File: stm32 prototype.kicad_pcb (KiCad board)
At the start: 4 copper layers, 137 x 54.5 mm, 114 parts, among them J1 USB_B_Mini, J2 Conn_01x06, J3 Conn_02x08_Odd_Even, J4 Conn_01x10, J5 Conn_02x04_Odd_Even, J6 Conn_01x15, J7 Conn_01x15, Q1 Q_NMOS_GSD, Q10 2N2219, Q11 Q_NMOS_GSD, Q2 Q_NMOS_GSD, Q3 Q_NMOS_GSD, Q4 Q_NMOS_GSD, Q5 Q_NMOS_GSD, Q6 Q_NMOS_GSD, Q7 Q_NMOS_GSD, Q8 Q_NMOS_GSD, Q9 2N2219, SW1 SW_Push, SW2 SW_Push, U1 FT232RL, U2 W25Q128JV-DTR, U3 STM32F407VGTx, U4 LD1117S33TR, U5 ESP32-WROOM, U7 TPS62203DBVR, Y1 Crystal_GND24

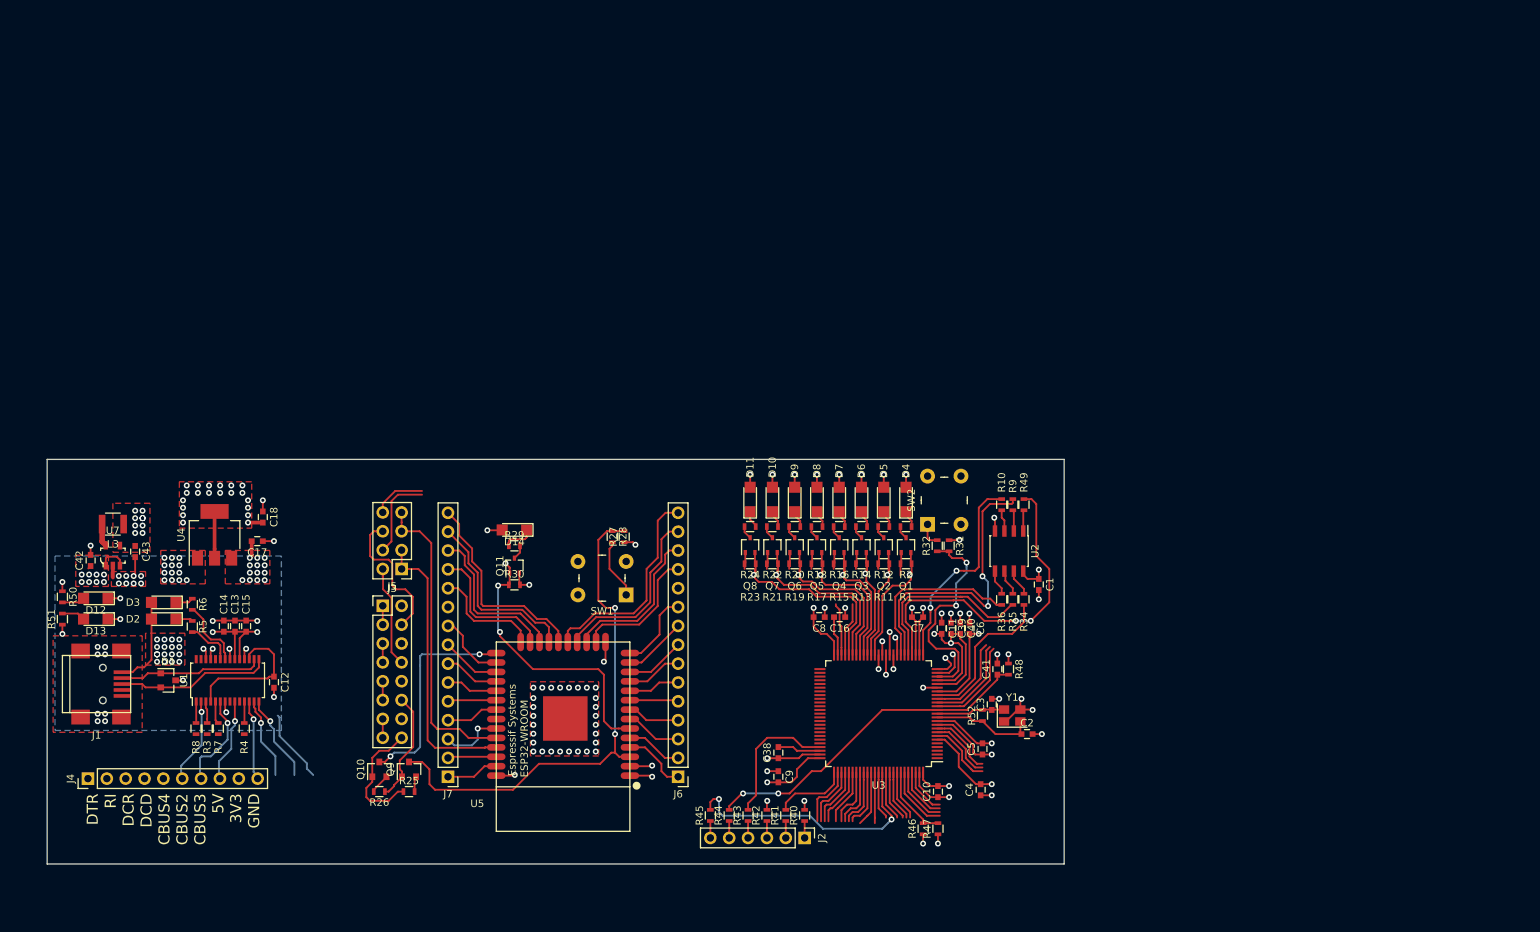
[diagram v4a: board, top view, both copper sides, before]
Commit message: layout almost done, changing my mind, getting rid of esp32, usb section
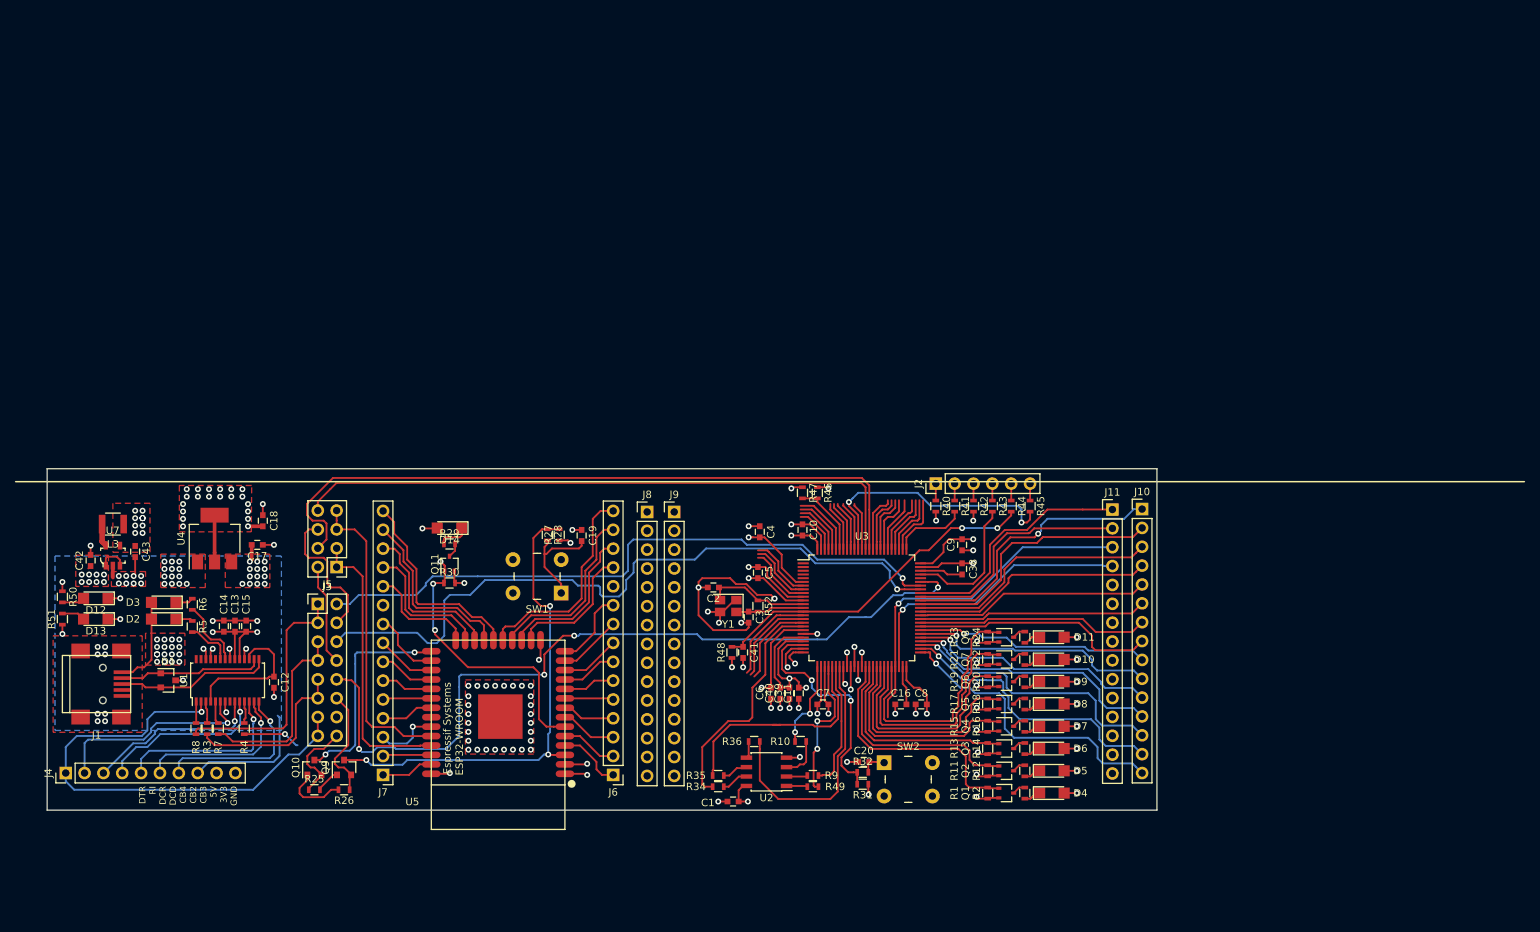
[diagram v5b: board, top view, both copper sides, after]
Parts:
- added C19: 0.1uF, Capacitors_SMD:C_0603, F.Cu at (134.5, 98.2)
- added C20: 0.1uF, Capacitors_SMD:C_0603, F.Cu at (172.5, 128.8)
- added J10: Conn_01x15, Pin_Headers:Pin_Header_Straight_1x15_Pitch2.54mm, F.Cu at (210.0, 94.7)
- added J11: Conn_01x15, Pin_Headers:Pin_Header_Straight_1x15_Pitch2.54mm, F.Cu at (206.0, 94.8)
- added J8: Conn_01x15, Pin_Headers:Pin_Header_Straight_1x15_Pitch2.54mm, F.Cu at (143.3, 95.1)
- added J9: Conn_01x15, Pin_Headers:Pin_Header_Straight_1x15_Pitch2.54mm, F.Cu at (147.0, 95.1)
- Q10, Q9: value 2N2219 -> Q_NPN_BEC
- R25, R26: value 12k -> 10k
- moved R45 59.9 mm to (194.9, 94.3), turned to 270 degrees
- moved R44 56.4 mm to (192.4, 94.3), turned to 270 degrees
- moved R43 53.1 mm to (189.8, 94.3), turned to 270 degrees
- moved J2 50.9 mm to (182.2, 91.3), turned to 90 degrees
- moved C1 50.5 mm to (154.9, 134.1), turned to 180 degrees
- moved R42 50.1 mm to (187.3, 94.3), turned to 270 degrees
- moved R47 48.8 mm to (164.2, 92.5), turned to 270 degrees
- moved R34 48.3 mm to (152.9, 132.1), turned to 0 degrees
- moved R41 47.5 mm to (184.8, 94.3), turned to 270 degrees
- moved R49 47.5 mm to (165.7, 132.1), turned to 180 degrees
- moved R46 47.4 mm to (166.2, 92.5), turned to 270 degrees
- moved C2 46.6 mm to (152.2, 105.2), turned to 180 degrees
- moved R35 46.2 mm to (152.9, 130.6), turned to 0 degrees
- moved C4 45.7 mm to (158.5, 97.8), turned to 270 degrees
- moved R9 45.4 mm to (165.7, 130.6), turned to 180 degrees
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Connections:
- Q10 pad 1: FTDI_ES_DTR -> Net-(Q10-Pad1)
- Q10 pad 2: Net-(Q10-Pad2) -> FTDI_ES_DTR
- Q9 pad 1: FTDI_ES_RTS -> Net-(Q9-Pad1)
- Q9 pad 2: Net-(Q9-Pad2) -> FTDI_ES_RTS
- R25 pad 2: Net-(Q9-Pad2) -> Net-(Q9-Pad1)
- R26 pad 2: Net-(Q10-Pad2) -> Net-(Q10-Pad1)
- R7 pad 1: FTDI_ST_RXD -> Net-(R7-Pad1)
- R7 pad 2: Net-(R7-Pad2) -> Net-(J3-Pad5)
- R8 pad 1: FTDI_ST_TXD -> Net-(R8-Pad1)
- R8 pad 2: Net-(R8-Pad2) -> Net-(J3-Pad1)
- U1 pad 1: Net-(J3-Pad1) -> Net-(R8-Pad1)
- U1 pad 5: Net-(J3-Pad5) -> Net-(R7-Pad1)
- U3 pad 47: (no net) -> PB10
- U3 pad 48: (no net) -> PB11
- U3 pad 51: (no net) -> PB12
- U3 pad 52: (no net) -> PB13
- U3 pad 53: (no net) -> PB14
- U3 pad 54: (no net) -> PB15
- U3 pad 55: (no net) -> PD8
- U3 pad 56: (no net) -> PD9
- U3 pad 57: (no net) -> PD10
- U3 pad 58: (no net) -> PD11
- U3 pad 59: (no net) -> PD12
- U3 pad 60: (no net) -> PD13
- U3 pad 61: (no net) -> PD14
- U3 pad 62: (no net) -> PD15
- U3 pad 63: (no net) -> PC6
- U3 pad 64: (no net) -> PC7
- U3 pad 65: (no net) -> PC8
- U3 pad 66: (no net) -> PC9
- U3 pad 67: (no net) -> PA8
- U3 pad 68: Net-(R7-Pad2) -> FTDI_ST_RXD
- U3 pad 69: Net-(R8-Pad2) -> FTDI_ST_TXD
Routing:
- net FTDI_ST_RTS: track 0.00 -> 109.1 mm, vias 0 -> 4
- net FTDI_ST_RXD: track 0.00 -> 94.7 mm, vias 0 -> 1
- net FTDI_ST_TXD: track 0.00 -> 87.5 mm, vias 0 -> 1
- net ST_ESP_RXD: track 19.0 -> 94.6 mm
- net ST_ESP_TXD: track 14.0 -> 84.6 mm
- net Net-(J3-Pad13): track 2.54 -> 67.2 mm, vias 0 -> 1
- net PB10: track 0.00 -> 47.9 mm, vias 0 -> 1
- net PB12: track 0.00 -> 40.2 mm, vias 0 -> 1
- net PB11: track 0.00 -> 38.6 mm, vias 0 -> 1
- net PB13: track 0.00 -> 38.3 mm, vias 0 -> 1
- net PC8: track 0.00 -> 37.6 mm, vias 0 -> 1
- net PB14: track 0.00 -> 37.2 mm, vias 0 -> 1
- net PC7: track 0.00 -> 36.2 mm
- net PB15: track 0.00 -> 35.4 mm, vias 0 -> 1
- net PC6: track 0.00 -> 34.3 mm
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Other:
- board size 137 x 54.5 mm -> 149.5 x 46 mm
- board text added: "DTR RI DCR DCD CB4 CB2 CB3 5V 3V3 GND"
- board text removed: "DTR RI DCR DCD CBUS4 CBUS2 CBUS3 5V 3V3 GND"

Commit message: Ordered PCB 12/18
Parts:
- removed C12, C13, C14, C15: C, Capacitors_SMD:C_0603
- removed C19: 0.1uF, Capacitors_SMD:C_0603
- removed D1: SP0502BAHT, TO_SOT_Packages_SMD:SOT-23
- removed D14, D2, D3: LED, LEDs:LED_1206
- removed J8: Conn_01x15, Pin_Headers:Pin_Header_Straight_1x15_Pitch2.54mm
- removed Q10, Q9: Q_NPN_BEC, TO_SOT_Packages_SMD:SOT-23
- removed Q11: Q_NMOS_GSD, TO_SOT_Packages_SMD:SOT-323_SC-70
- removed R25, R26: 10k, Resistors_SMD:R_0603
- removed R27: 12k, Resistors_SMD:R_0603
- removed R28: 470R, Resistors_SMD:R_0603
- removed R29, R5, R6: 330R, Resistors_SMD:R_0603
- removed R30: 10K, Resistors_SMD:R_0603
- removed R7, R8: 0R, Resistors_SMD:R_0603
- removed SW1: SW_Push, switches_mdg:Switch_Tactile_6x6mm_Vertical_SMD_MJTP1230
- removed U1: FT232RL, Housings_SSOP:TSSOP-28_4.4x9.7mm_Pitch0.65mm
- removed U5: ESP32-WROOM, ESP32-footprints-Lib:ESP32-WROOM
- added J12: Conn_01x07, Pin_Headers:Pin_Header_Straight_1x07_Pitch2.54mm, F.Cu at (203.2, 127.0)
- added J13: Conn_01x06, Pin_Headers:Pin_Header_Straight_1x06_Pitch2.54mm, F.Cu at (170.2, 127.0)
- added J14: Conn_01x30, Pin_Headers:Pin_Header_Straight_1x30_Pitch2.54mm, F.Cu at (139.7, 68.6)
- J1: value USB_B_Mini -> Conn_01x04; footprint Connectors:USB_Mini-B -> Pin_Headers:Pin_Header_Straight_1x04_Pitch2.54mm
- J10: value Conn_01x15 -> Conn_01x03; footprint Pin_Headers:Pin_Header_Straight_1x15_Pitch2.54mm -> Pin_Headers:Pin_Header_Straight_1x03_Pitch2.54mm
- J11: value Conn_01x15 -> Conn_01x05; footprint Pin_Headers:Pin_Header_Straight_1x15_Pitch2.54mm -> Pin_Headers:Pin_Header_Straight_1x05_Pitch2.54mm
- J3: value Conn_02x08_Odd_Even -> Conn_01x08; footprint Pin_Headers:Pin_Header_Straight_2x08_Pitch2.54mm -> Pin_Headers:Pin_Header_Straight_1x08_Pitch2.54mm
- J4: value Conn_01x10 -> Conn_01x06; footprint Pin_Headers:Pin_Header_Straight_1x10_Pitch2.54mm -> Pin_Headers:Pin_Header_Straight_1x06_Pitch2.54mm
- J5: value Conn_02x04_Odd_Even -> Conn_01x06; footprint Pin_Headers:Pin_Header_Straight_2x04_Pitch2.54mm -> Pin_Headers:Pin_Header_Straight_1x06_Pitch2.54mm
- J6, J7: value Conn_01x15 -> Conn_01x06; footprint Pin_Headers:Pin_Header_Straight_1x15_Pitch2.54mm -> Pin_Headers:Pin_Header_Straight_1x06_Pitch2.54mm
- J9: value Conn_01x15 -> Conn_01x08; footprint Pin_Headers:Pin_Header_Straight_1x15_Pitch2.54mm -> Pin_Headers:Pin_Header_Straight_1x08_Pitch2.54mm
- R3, R4: value 0R -> 10K
- moved J4 144.0 mm to (207.6, 110.3), turned to 0 degrees
- moved R3 137.8 mm to (220.5, 105.0), turned to 270 degrees
- moved R4 130.8 mm to (218.8, 107.5), turned to 0 degrees
- moved J7 112.6 mm to (218.5, 110.3), turned to 0 degrees
- moved J5 110.0 mm to (211.2, 110.3), turned to 0 degrees
- moved D12 85.2 mm to (154.3, 105.9)
- moved D13 85.2 mm to (154.3, 108.7)
- moved R50 85.2 mm to (149.8, 105.7)
- moved R51 85.2 mm to (149.8, 108.7)
- moved J6 78.8 mm to (214.9, 110.3), turned to 0 degrees
- moved C1 75.8 mm to (202.1, 74.7), turned to 0 degrees
- moved R34 75.4 mm to (204.1, 76.7), turned to 180 degrees
- moved C42 74.7 mm to (143.0, 98.4), turned to 180 degrees
- moved U7 73.8 mm to (144.9, 95.2), turned to 90 degrees
- moved J9 73.3 mm to (219.0, 81.7)
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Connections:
- net ST_MISO renamed SPI1_MISO
- net ST_MOSI renamed SPI1_MOSI
- net ST_SCK renamed SPI1_SCK
- J1 pad 1: +5V -> GND
- J1 pad 2: Net-(D1-Pad1) -> (no net)
- J1 pad 3: Net-(D1-Pad2) -> FTDI_ST_TXD
- J1 pad 4: (no net) -> FTDI_ST_RXD
- J10 pad 1: PC8 -> PD0
- J10 pad 2: PC7 -> PD1
- J10 pad 3: PC6 -> PD2
- J11 pad 1: PA8 -> PB4
- J11 pad 2: PC9 -> PB8
- J11 pad 3: PB10 -> PB9
- J11 pad 4: PB11 -> PE0
- J11 pad 5: (no net) -> PE1
- J3 pad 1: Net-(J3-Pad1) -> +5V
- J3 pad 2: FTDI_ST_TXD -> (no net)
- J3 pad 3: Net-(J3-Pad1) -> (no net)
- J3 pad 4: FTDI_ES_TXD -> (no net)
- J3 pad 5: Net-(J3-Pad5) -> (no net)
- J3 pad 6: FTDI_ST_RXD -> FTDI_ST_RTS
- J3 pad 7: Net-(J3-Pad5) -> FTDI_CTS
- J3 pad 8: FTDI_ES_RXD -> GND
- J4 pad 1: Net-(J3-Pad13) -> I2C1_SDA
- J4 pad 2: FTDI_RI -> I2C1_SCL
- J4 pad 3: FTDI_DCR -> I2C1_SMBA
- J4 pad 4: FTDI_DCD -> +5V
- J4 pad 5: FTDI_CBUS4 -> +3V3
- J4 pad 6: FTDI_CBUS2 -> GND
- J5 pad 1: Net-(J5-Pad1) -> I2C1_SDA
- J5 pad 2: FTDI_ES_RXD -> I2C1_SCL
- J5 pad 3: Net-(J5-Pad1) -> I2C1_SMBA
- J5 pad 4: ST_ESP_RXD -> +5V
- J5 pad 5: Net-(J5-Pad5) -> +3V3
- J5 pad 6: FTDI_ES_TXD -> GND
- J6 pad 1: SENSOR_VP -> I2C1_SDA
- J6 pad 2: SENSOR_VN -> I2C1_SCL
- J6 pad 3: IO35 -> I2C1_SMBA
- J6 pad 4: IO32 -> +5V
- J6 pad 5: IO33 -> +3V3
- J6 pad 6: IO25 -> GND
- J7 pad 1: IO23 -> I2C1_SDA
- J7 pad 2: IO22 -> I2C1_SCL
- J7 pad 3: IO21 -> I2C1_SMBA
- J7 pad 4: IO19 -> +5V
- J7 pad 5: IO18 -> +3V3
- J7 pad 6: IO5 -> GND
- J9 pad 1: (no net) -> PC15
- J9 pad 2: (no net) -> PC14
- J9 pad 3: (no net) -> PC13
- J9 pad 4: (no net) -> PE6
- J9 pad 5: (no net) -> PE5
- J9 pad 6: (no net) -> PE4
- J9 pad 7: (no net) -> PE3
- J9 pad 8: (no net) -> PE2
- R3 pad 1: Net-(J3-Pad11) -> +3V3
- R3 pad 2: Net-(R3-Pad2) -> I2C1_SCL
- R4 pad 1: FTDI_CTS -> +3V3
- R4 pad 2: Net-(R4-Pad2) -> I2C1_SDA
- U3 pad 1: (no net) -> PE2
- U3 pad 15: (no net) -> PC0
- U3 pad 16: (no net) -> PC1
- U3 pad 17: (no net) -> PC2
- U3 pad 2: (no net) -> PE3
- U3 pad 24: (no net) -> PA1
- U3 pad 25: (no net) -> PA2
- U3 pad 3: (no net) -> PE4
- U3 pad 33: (no net) -> PC4
- U3 pad 34: (no net) -> PC5
- U3 pad 35: (no net) -> PB0
- U3 pad 36: (no net) -> PB1
- U3 pad 37: (no net) -> PB2
- U3 pad 38: (no net) -> PE7
- U3 pad 39: STATUS_BIT0 -> PE8
- U3 pad 4: (no net) -> PE5
- U3 pad 40: STATUS_BIT1 -> PE9
- U3 pad 41: STATUS_BIT2 -> PE10
- U3 pad 42: STATUS_BIT3 -> PE11
- U3 pad 43: STATUS_BIT4 -> PE12
- U3 pad 44: STATUS_BIT5 -> PE13
- U3 pad 45: STATUS_BIT6 -> PE14
- U3 pad 46: STATUS_BIT7 -> PE15
- U3 pad 5: (no net) -> PE6
- U3 pad 60: PD13 -> STATUS_BIT0
- U3 pad 61: PD14 -> STATUS_BIT1
- U3 pad 62: PD15 -> STATUS_BIT2
- U3 pad 63: PC6 -> STATUS_BIT3
- U3 pad 64: PC7 -> STATUS_BIT4
- U3 pad 65: PC8 -> STATUS_BIT5
- U3 pad 66: PC9 -> STATUS_BIT6
- U3 pad 67: PA8 -> STATUS_BIT7
- U3 pad 7: (no net) -> PC13
- U3 pad 77: (no net) -> SPI3_NSS
- U3 pad 78: (no net) -> SPI3_SCK
- U3 pad 79: (no net) -> SPI3_MISO
- U3 pad 8: (no net) -> PC14
- U3 pad 80: (no net) -> SPI3_MOSI
- U3 pad 81: (no net) -> PD0
- U3 pad 82: (no net) -> PD1
- U3 pad 83: (no net) -> PD2
- U3 pad 84: (no net) -> USART2_CTS
- U3 pad 85: (no net) -> USART2_RTS
- U3 pad 86: ST_ESP_RXD -> USART2_TX
- U3 pad 87: ST_ESP_TXD -> USART2_RX
- U3 pad 88: (no net) -> USART2_CK
- U3 pad 9: (no net) -> PC15
- U3 pad 90: (no net) -> PB4
- U3 pad 91: (no net) -> I2C1_SMBA
- U3 pad 92: (no net) -> I2C1_SCL
- U3 pad 93: (no net) -> I2C1_SDA
- U3 pad 95: (no net) -> PB8
- U3 pad 96: (no net) -> PB9
- U3 pad 97: (no net) -> PE0
- U3 pad 98: (no net) -> PE1
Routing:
- net (no net): track 220.7 -> 0.00 mm, vias 8 -> 0
- net ST_ESP_RXD: track 94.6 -> 0.00 mm
- net FTDI_ST_RTS: track 109.1 -> 24.2 mm, vias 4 -> 0
- net ST_ESP_TXD: track 84.6 -> 0.00 mm
- net Net-(J3-Pad13): track 67.2 -> 0.00 mm, vias 1 -> 0
- net ESP_EN: track 66.9 -> 0.00 mm, vias 3 -> 0
- net +5V: track 51.7 -> 116.1 mm, vias 42 -> 22
- net I2C1_SCL: track 0.00 -> 52.5 mm
- net PC15: track 0.00 -> 50.6 mm
- net PC14: track 0.00 -> 49.4 mm
- net FTDI_ST_RXD: track 94.7 -> 45.5 mm, vias 1 -> 0
- net I2C1_SDA: track 0.00 -> 48.7 mm
- net FTDI_ST_TXD: track 87.5 -> 39.9 mm, vias 1 -> 0
- net PE4: track 0.00 -> 47.3 mm, vias 0 -> 2
- net PC13: track 0.00 -> 46.8 mm
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- added copper zone on B.Cu, net GND
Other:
- board size 149.5 x 46 mm -> 86 x 64 mm
- rule pad_to_mask_clearance: 0.051 -> 0
- board text added: "5V"
- board text added: "GND X RXD TXD"
- board text added: "I2C1 SDA SCL SMBA 5V 3V3 GND"
- board text added: "PA1"
- board text added: "PA2"
- board text added: "PB0"
- board text added: "PB1"
- board text added: "PB10"
- board text added: "PB11"
- board text added: "PB12"
- board text added: "PB13"
- board text added: "PB14"
- board text added: "PB15"
- board text added: "PB2"
- board text added: "PB4 PB8 PB9 PE0 PE1"
- board text added: "PC0"
- board text added: "PC1"
- board text added: "PC2"
- board text added: "PC4"
- board text added: "PC5"
- board text added: "PD10"
- board text added: "PD11"
- board text added: "PD12"
- board text added: "PD2 PD1 PD0"
- board text added: "PD8"
- board text added: "PD9"
- board text added: "PE10"
- board text added: "PE11"
- board text added: "PE12"
- board text added: "PE13"
- board text added: "PE14"
- board text added: "PE15"
- board text added: "PE7"
- board text added: "PE8"
- board text added: "PE9"
- board text added: "RTS CTS GND"
- board text added: "SPI3 NSS SCK MISO MOSI 3V3 GND"
- board text added: "SWO NRST TMS_SDIO GND TCK_SWCK GND"
- board text added: "USART2 GND 3V3 CTS RTS TX RX CK"
- board text removed: "DTR RI DCR DCD CB4 CB2 CB3 5V 3V3 GND"

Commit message: pushed change to stm32f405 to pcb
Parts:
- removed J11: Conn_01x05, Pin_Headers:Pin_Header_Straight_1x05_Pitch2.54mm
- removed R10, R34, R35, R36, R40, R41, R42, R43, R44, R45, R49, R9: 0R, Resistors_SMD:R_0603
- removed U2: W25Q128JV-DTR, Housings_SOIC:SOIC-8_3.9x4.9mm_Pitch1.27mm
- removed U4: LD1117S33TR, TO_SOT_Packages_SMD:SOT-223
- added C12: 0.1uF, Capacitors_SMD:C_0603, F.Cu at (91.0, 84.8)
- added C13: 2.2uF, Capacitors_SMD:C_0603, F.Cu at (93.9, 84.8)
- added C14: 2.2uF, Capacitors_SMD:C_0603, F.Cu at (96.7, 84.8)
- added C15: 9pF, Capacitors_SMD:C_0603, F.Cu at (91.0, 86.2)
- added C19: .1uF, Capacitors_SMD:C_0603, F.Cu at (93.9, 86.2)
- added C21: .1uF, Capacitors_SMD:C_0603, F.Cu at (96.7, 86.2)
- added C22: .1uF, Capacitors_SMD:C_0603, F.Cu at (99.6, 84.8)
- added C23: .1uF, Capacitors_SMD:C_0603, F.Cu at (99.6, 86.2)
- added C24: .1uF, Capacitors_SMD:C_0603, F.Cu at (102.4, 84.8)
- added J8: Conn_ARM_JTAG_SWD_10, Pin_Headers:Pin_Header_Straight_2x05_Pitch1.27mm_SMD, F.Cu at (121.4, 65.8)
- added R5: 10k, Resistors_SMD:R_0603, F.Cu at (104.3, 77.4)
- added R6: 10k, Resistors_SMD:R_0603, F.Cu at (104.3, 78.9)
- added R7: 1MR, Resistors_SMD:R_0603, F.Cu at (104.3, 80.4)
- added R8: 10k, Resistors_SMD:R_0603, F.Cu at (104.3, 81.9)
- added SW1: SW_Push, switches_mdg:Switch_Tactile_6x6mm_Vertical_SMD_MJTP1230, F.Cu at (89.9, 80.2)
- added Y2: Crystal_GND24, Crystals:Crystal_SMD_SeikoEpson_TSX3225-4pin_3.2x2.5mm, F.Cu at (87.5, 85.5)
- C1: value C -> 4.7uF
- C10, C11, C41, C5, C6, C7, C8, C9: value C -> .1uF
- C17: value 0.1uF -> 9pF
- C18: value 10uF -> .1uF
- C2, C3: value C -> 9pF
- C4: value C -> 1uF
- J2: value Conn_01x06 -> Conn_02x05_Odd_Even; footprint Pin_Headers:Pin_Header_Straight_1x06_Pitch2.54mm -> Pin_Headers:Pin_Header_Straight_2x05_Pitch1.27mm_SMD
- J9: value Conn_01x08 -> Conn_01x03
- R31: value 12k -> 10k
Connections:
- C1 pad 1: +3V3 -> GND
- C1 pad 2: GND -> +3V3
- C17 pad 1: GND -> Net-(C17-Pad1)
- C17 pad 2: +5V -> GND
- J10 pad 1: PD0 -> GND
- J10 pad 2: PD1 -> Net-(J10-Pad2)
- J10 pad 3: PD2 -> +3V3
- J2 pad 1: Net-(J2-Pad1) -> +3V3
- J2 pad 2: Net-(J2-Pad2) -> TMS_SWDIO
- J2 pad 3: Net-(J2-Pad3) -> GND
- J2 pad 4: Net-(J2-Pad4) -> TCK_SWCLK
- J2 pad 5: Net-(J2-Pad5) -> GND
- J2 pad 6: Net-(J2-Pad6) -> SWO
- J9 pad 1: PC15 -> GND
- J9 pad 2: PC14 -> Net-(J9-Pad2)
- J9 pad 3: PC13 -> +3V3
- J9 pad 4: PE6 -> (no net)
- J9 pad 5: PE5 -> (no net)
- J9 pad 6: PE4 -> (no net)
- J9 pad 7: PE3 -> (no net)
- J9 pad 8: PE2 -> (no net)
- U3 pad 1: PE2 -> (no net)
- U3 pad 18: ST_HOLD -> (no net)
- U3 pad 2: PE3 -> (no net)
- U3 pad 23: Net-(R31-Pad2) -> (no net)
- U3 pad 26: ST_WP -> (no net)
- U3 pad 29: MEM_CHIP_SELECT -> (no net)
- U3 pad 3: PE4 -> (no net)
- U3 pad 30: SPI1_SCK -> (no net)
- U3 pad 31: SPI1_MISO -> (no net)
- U3 pad 32: SPI1_MOSI -> (no net)
- U3 pad 4: PE5 -> (no net)
- U3 pad 5: PE6 -> (no net)
- U3 pad 7: PC13 -> (no net)
- U3 pad 8: PC14 -> (no net)
- U3 pad 81: PD0 -> (no net)
- U3 pad 82: PD1 -> (no net)
- U3 pad 83: PD2 -> (no net)
- U3 pad 9: PC15 -> (no net)
- U3 pad 90: PB4 -> (no net)
- U3 pad 95: PB8 -> (no net)
- U3 pad 96: PB9 -> (no net)
- U3 pad 97: PE0 -> (no net)
- U3 pad 98: PE1 -> (no net)
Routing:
- net (no net): track 0.00 -> 435.2 mm, vias 0 -> 13
- net GND: track 128.8 -> 199.1 mm
- net +3V3: track 139.9 -> 194.3 mm
- net PC15: track 50.6 -> 0.00 mm
- net PC14: track 49.4 -> 0.00 mm
- net Net-(J9-Pad2): track 0.00 -> 49.4 mm
- net PE4: track 47.3 -> 0.00 mm, vias 2 -> 0
- net PC13: track 46.8 -> 0.00 mm
- net PE6: track 46.1 -> 0.00 mm, vias 1 -> 0
- net PE2: track 40.6 -> 0.00 mm
- net PE3: track 39.3 -> 0.00 mm
- net PE5: track 38.3 -> 0.00 mm, vias 2 -> 0
- net SPI1_MOSI: track 34.4 -> 0.00 mm
- net ST_HOLD: track 31.7 -> 0.00 mm
- net SPI1_SCK: track 30.4 -> 0.00 mm
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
